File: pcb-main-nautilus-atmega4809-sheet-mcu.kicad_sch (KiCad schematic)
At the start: 20 parts, among them SW1 PTS645SH43SMTR92 LFS, U4 ATmega4809-A

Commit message: Update schematic annotations
Supports #2.
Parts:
- renumbered R13 to R12, R14 to R13, R12 to R14
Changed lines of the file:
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@@
   (symbol (lib_id "Device:R_Small") (at 66.04 113.03 180) (unit 1)
     (in_bom yes) (on_board yes) (fields_autoplaced)
-    (property "Reference" "R12" (id 0) (at 68.58 111.7599 0)
+    (property "Reference" "R14" (id 0) (at 68.58 111.7599 0)
       (effects (font (size 1.27 1.27)) (justify right))
     )
@@
   (symbol (lib_id "Device:R_Small") (at 167.64 105.41 0) (unit 1)
     (in_bom yes) (on_board yes) (fields_autoplaced)
-    (property "Reference" "R13" (id 0) (at 170.18 104.1399 0)
+    (property "Reference" "R12" (id 0) (at 170.18 104.1399 0)
       (effects (font (size 1.27 1.27)) (justify left))
     )
@@
   (symbol (lib_id "Device:R_Small") (at 182.88 105.41 0) (unit 1)
     (in_bom yes) (on_board yes) (fields_autoplaced)
-    (property "Reference" "R14" (id 0) (at 185.42 104.1399 0)
-      (effects (font (size 1.27 1.27)) (justify left))
-    )
+    (property "Reference" "R13" (id 0) (at 185.42 104.1399 0)
+      (effects (font (size 1.27 1.27)) (justify left))
+    )

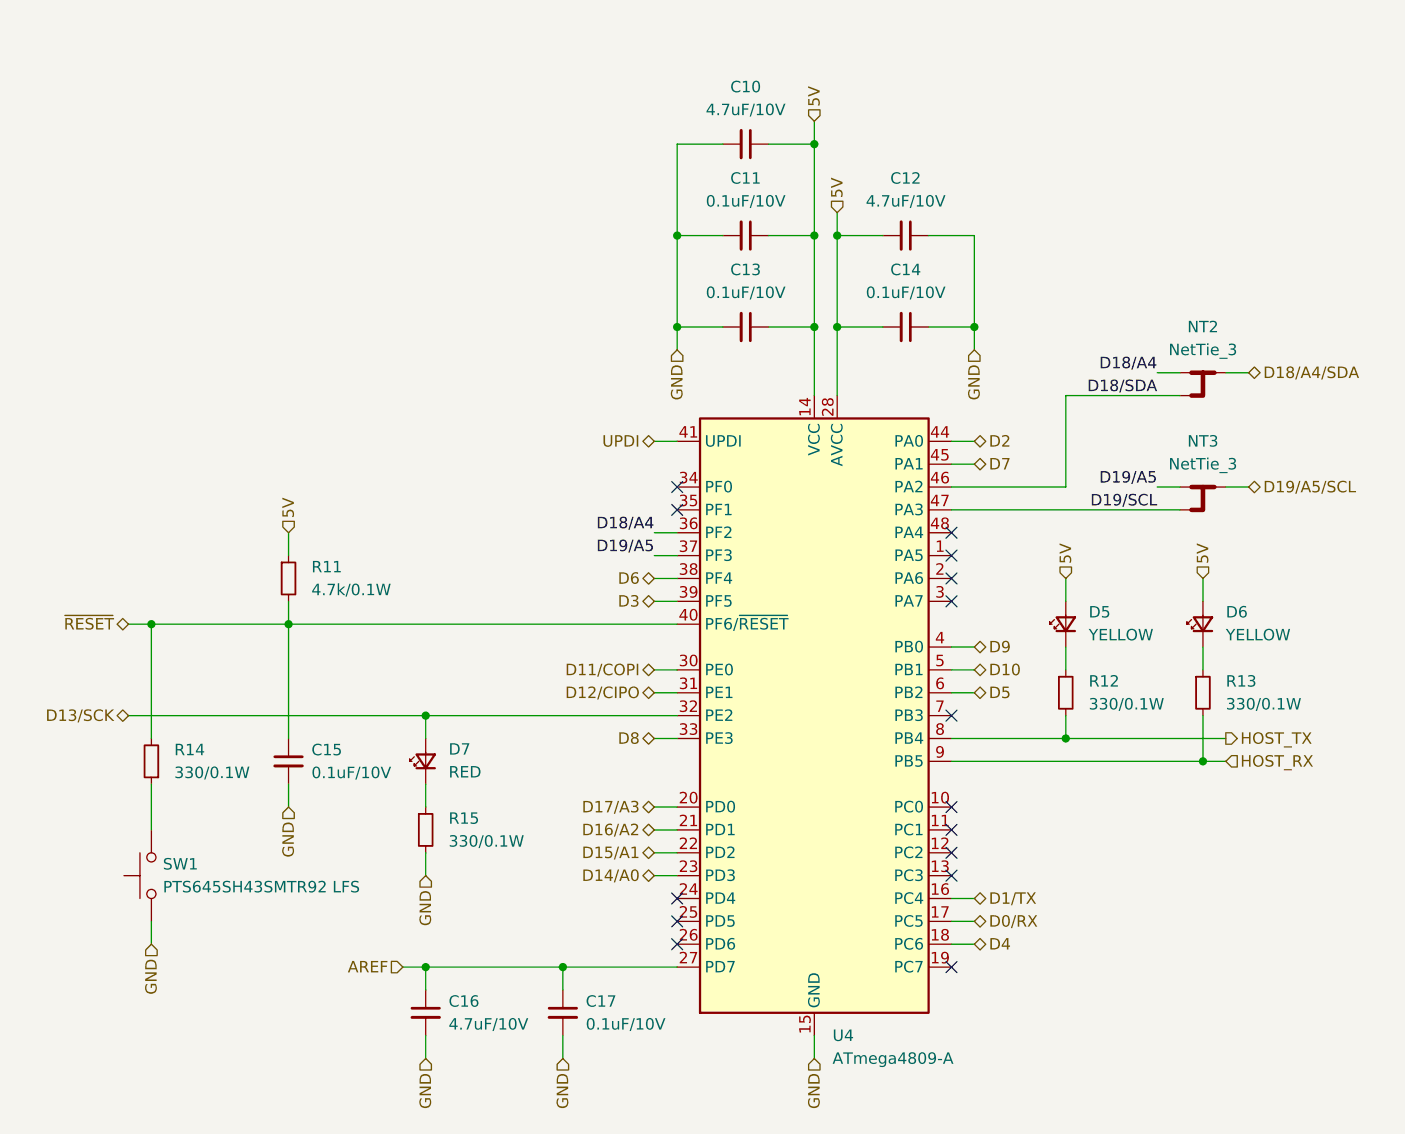
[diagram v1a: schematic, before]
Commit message: Connect root sheet
Supports #2.
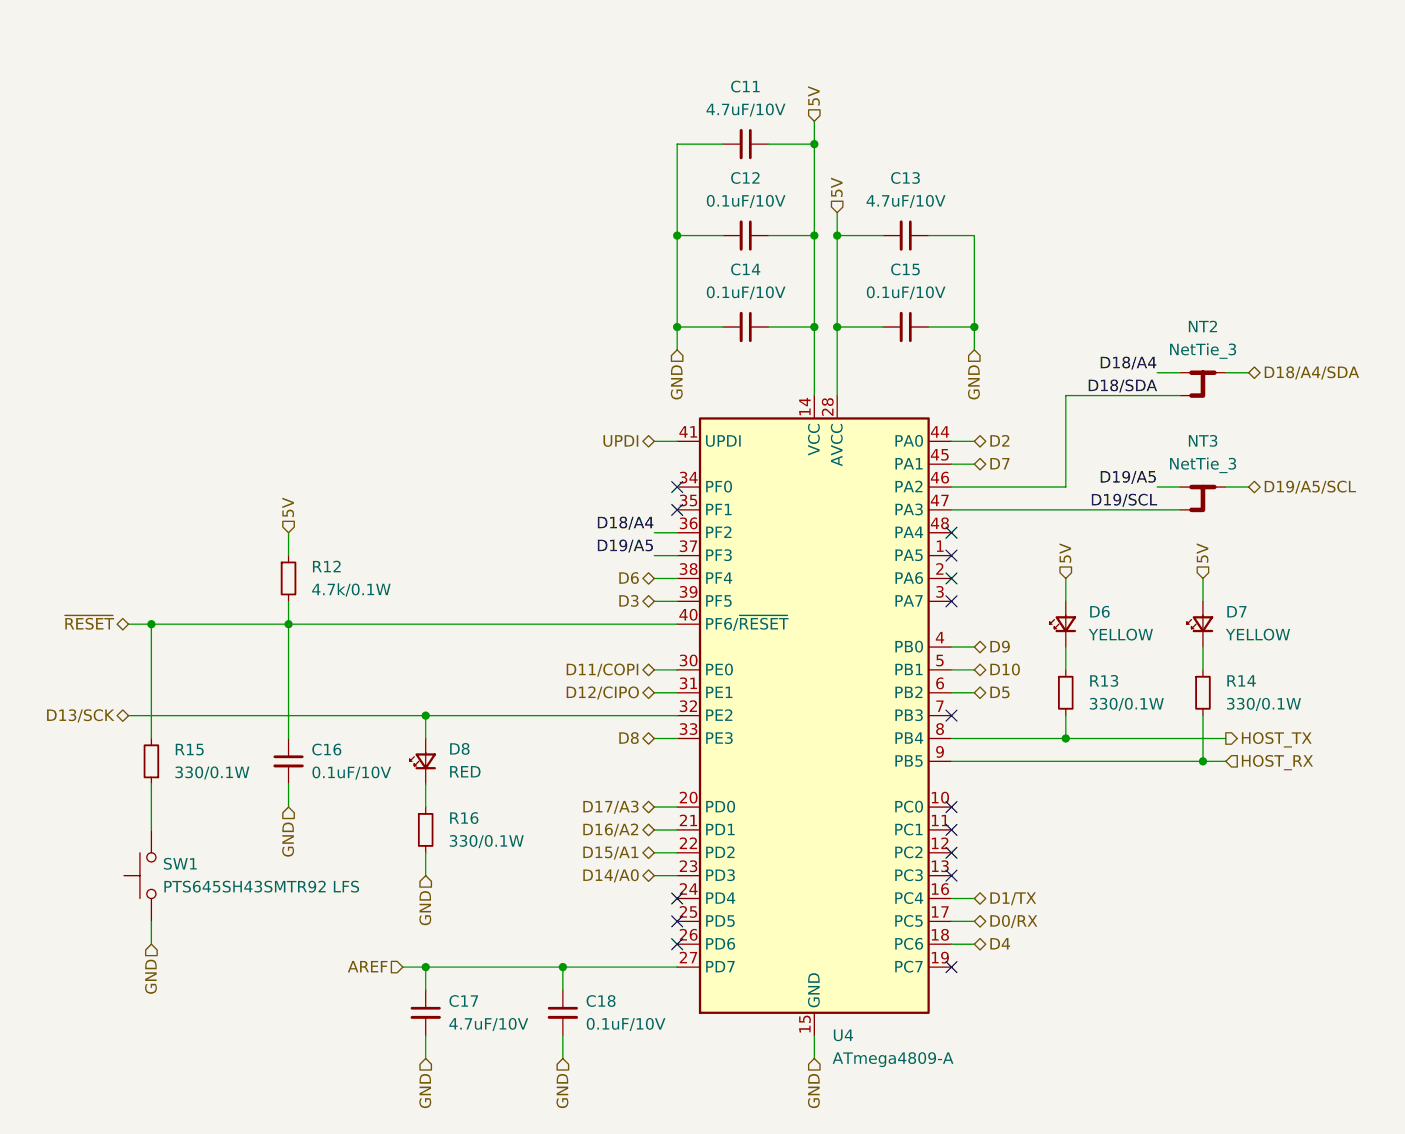
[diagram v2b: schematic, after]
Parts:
- renumbered C10 to C11, C11 to C12, C12 to C13, C13 to C14, C14 to C15, C15 to C16, C16 to C17, C17 to C18, D5 to D6, D6 to D7, D7 to D8, R11 to R12, R12 to R13, R13 to R14, R14 to R15, R15 to R16
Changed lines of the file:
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@@
   (symbol (lib_id "Device:R_Small") (at 96.52 120.65 0) (unit 1)
     (in_bom yes) (on_board yes) (fields_autoplaced)
-    (property "Reference" "R15" (id 0) (at 99.06 119.3799 0)
+    (property "Reference" "R16" (id 0) (at 99.06 119.3799 0)
       (effects (font (size 1.27 1.27)) (justify left))
     )
@@
   (symbol (lib_id "Device:C_Small") (at 111.76 140.97 0) (unit 1)
     (in_bom yes) (on_board yes) (fields_autoplaced)
-    (property "Reference" "C17" (id 0) (at 114.3 139.7062 0)
+    (property "Reference" "C18" (id 0) (at 114.3 139.7062 0)
       (effects (font (size 1.27 1.27)) (justify left))
     )
@@
   (symbol (lib_id "Device:C_Small") (at 149.86 64.77 270) (unit 1)
     (in_bom yes) (on_board yes) (fields_autoplaced)
-    (property "Reference" "C14" (id 0) (at 149.8536 58.42 90))
+    (property "Reference" "C15" (id 0) (at 149.8536 58.42 90))
     (property "Value" "0.1uF/10V" (id 1) (at 149.8536 60.96 90))
     (property "Footprint" "Capacitor_SMD:C_0603_1608Metric_Pad1.08x0.95mm_HandSolder" (id 2) (at 149.86 64.77 0)
@@
   (symbol (lib_id "Device:C_Small") (at 132.08 64.77 270) (unit 1)
     (in_bom yes) (on_board yes) (fields_autoplaced)
-    (property "Reference" "C13" (id 0) (at 132.0736 58.42 90))
+    (property "Reference" "C14" (id 0) (at 132.0736 58.42 90))
     (property "Value" "0.1uF/10V" (id 1) (at 132.0736 60.96 90))
     (property "Footprint" "Capacitor_SMD:C_0603_1608Metric_Pad1.08x0.95mm_HandSolder" (id 2) (at 132.08 64.77 0)
@@
   (symbol (lib_id "Device:R_Small") (at 66.04 113.03 180) (unit 1)
     (in_bom yes) (on_board yes) (fields_autoplaced)
-    (property "Reference" "R14" (id 0) (at 68.58 111.7599 0)
+    (property "Reference" "R15" (id 0) (at 68.58 111.7599 0)
       (effects (font (size 1.27 1.27)) (justify right))
     )
@@
   (symbol (lib_id "Device:C_Small") (at 96.52 140.97 0) (unit 1)
     (in_bom yes) (on_board yes) (fields_autoplaced)
-    (property "Reference" "C16" (id 0) (at 99.06 139.7062 0)
+    (property "Reference" "C17" (id 0) (at 99.06 139.7062 0)
       (effects (font (size 1.27 1.27)) (justify left))
     )
@@
   (symbol (lib_id "Device:C_Small") (at 81.28 113.03 0) (unit 1)
     (in_bom yes) (on_board yes) (fields_autoplaced)
-    (property "Reference" "C15" (id 0) (at 83.82 111.7662 0)
+    (property "Reference" "C16" (id 0) (at 83.82 111.7662 0)
       (effects (font (size 1.27 1.27)) (justify left))
     )
@@
   (symbol (lib_id "Device:LED_Small") (at 167.64 97.79 90) (unit 1)
     (in_bom yes) (on_board yes) (fields_autoplaced)
-    (property "Reference" "D5" (id 0) (at 170.18 96.4564 90)
+    (property "Reference" "D6" (id 0) (at 170.18 96.4564 90)
       (effects (font (size 1.27 1.27)) (justify right))
     )
@@
   (symbol (lib_id "Device:R_Small") (at 167.64 105.41 0) (unit 1)
     (in_bom yes) (on_board yes) (fields_autoplaced)
-    (property "Reference" "R12" (id 0) (at 170.18 104.1399 0)
+    (property "Reference" "R13" (id 0) (at 170.18 104.1399 0)
       (effects (font (size 1.27 1.27)) (justify left))
     )
@@
   (symbol (lib_id "Device:LED_Small") (at 96.52 113.03 90) (unit 1)
     (in_bom yes) (on_board yes) (fields_autoplaced)
-    (property "Reference" "D7" (id 0) (at 99.06 111.6964 90)
+    (property "Reference" "D8" (id 0) (at 99.06 111.6964 90)
       (effects (font (size 1.27 1.27)) (justify right))
     )
@@
   (symbol (lib_id "Device:C_Small") (at 132.08 54.61 270) (unit 1)
     (in_bom yes) (on_board yes) (fields_autoplaced)
-    (property "Reference" "C11" (id 0) (at 132.0736 48.26 90))
+    (property "Reference" "C12" (id 0) (at 132.0736 48.26 90))
     (property "Value" "0.1uF/10V" (id 1) (at 132.0736 50.8 90))
     (property "Footprint" "Capacitor_SMD:C_0603_1608Metric_Pad1.08x0.95mm_HandSolder" (id 2) (at 132.08 54.61 0)
@@
   (symbol (lib_id "Device:C_Small") (at 132.08 44.45 270) (unit 1)
     (in_bom yes) (on_board yes) (fields_autoplaced)
-    (property "Reference" "C10" (id 0) (at 132.0736 38.1 90))
+    (property "Reference" "C11" (id 0) (at 132.0736 38.1 90))
     (property "Value" "4.7uF/10V" (id 1) (at 132.0736 40.64 90))
     (property "Footprint" "Capacitor_SMD:C_0603_1608Metric_Pad1.08x0.95mm_HandSolder" (id 2) (at 132.08 44.45 0)
@@
   (symbol (lib_id "Device:R_Small") (at 182.88 105.41 0) (unit 1)
     (in_bom yes) (on_board yes) (fields_autoplaced)
-    (property "Reference" "R13" (id 0) (at 185.42 104.1399 0)
+    (property "Reference" "R14" (id 0) (at 185.42 104.1399 0)
       (effects (font (size 1.27 1.27)) (justify left))
     )
@@
   (symbol (lib_id "Device:LED_Small") (at 182.88 97.79 90) (unit 1)
     (in_bom yes) (on_board yes) (fields_autoplaced)
-    (property "Reference" "D6" (id 0) (at 185.42 96.4564 90)
+    (property "Reference" "D7" (id 0) (at 185.42 96.4564 90)
       (effects (font (size 1.27 1.27)) (justify right))
     )
@@
   (symbol (lib_id "Device:C_Small") (at 149.86 54.61 270) (unit 1)
     (in_bom yes) (on_board yes) (fields_autoplaced)
-    (property "Reference" "C12" (id 0) (at 149.8536 48.26 90))
+    (property "Reference" "C13" (id 0) (at 149.8536 48.26 90))
     (property "Value" "4.7uF/10V" (id 1) (at 149.8536 50.8 90))
     (property "Footprint" "Capacitor_SMD:C_0603_1608Metric_Pad1.08x0.95mm_HandSolder" (id 2) (at 149.86 54.61 0)
@@
   (symbol (lib_id "Device:R_Small") (at 81.28 92.71 0) (unit 1)
     (in_bom yes) (on_board yes) (fields_autoplaced)
-    (property "Reference" "R11" (id 0) (at 83.82 91.4399 0)
-      (effects (font (size 1.27 1.27)) (justify left))
-    )
+    (property "Reference" "R12" (id 0) (at 83.82 91.4399 0)
+      (effects (font (size 1.27 1.27)) (justify left))
+    )

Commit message: Nest level shifter sheets under UPDI programmer and bridge sheet
Supports #2.
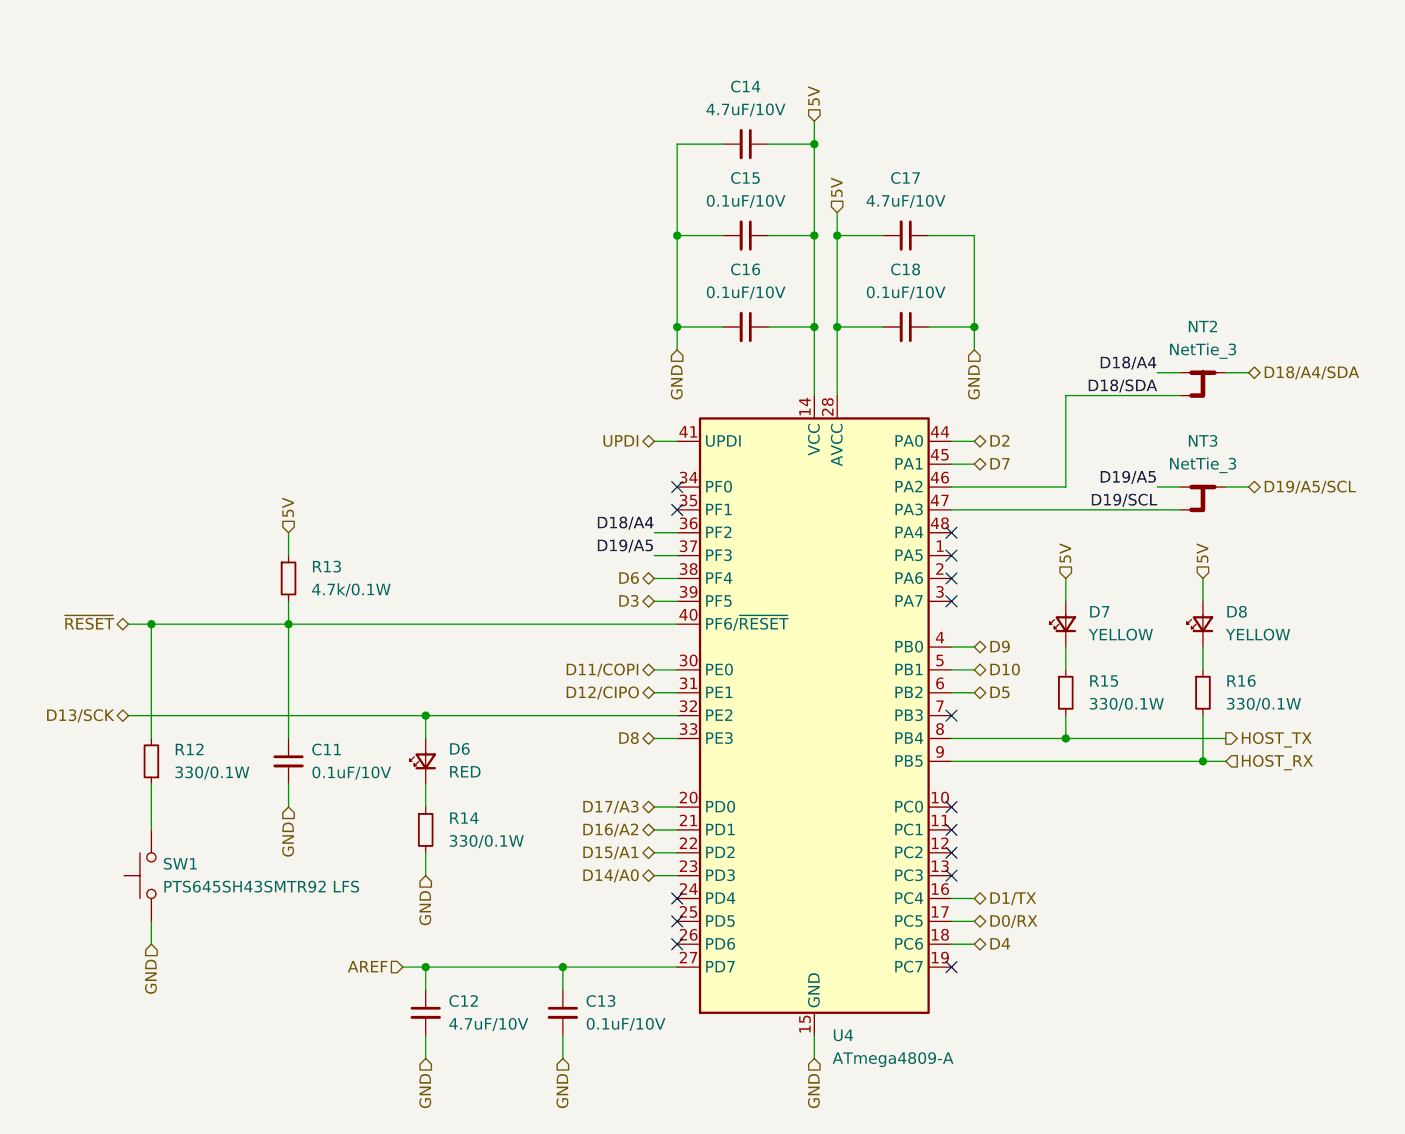
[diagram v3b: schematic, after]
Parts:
- renumbered C16 to C11, C17 to C12, C18 to C13, C11 to C14, C12 to C15, C14 to C16, C13 to C17, C15 to C18, D8 to D6, D6 to D7, D7 to D8, R15 to R12, R12 to R13, R16 to R14, R13 to R15, R14 to R16
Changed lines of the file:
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@@
   (symbol (lib_id "Device:R_Small") (at 96.52 120.65 0) (unit 1)
     (in_bom yes) (on_board yes) (fields_autoplaced)
-    (property "Reference" "R16" (id 0) (at 99.06 119.3799 0)
+    (property "Reference" "R14" (id 0) (at 99.06 119.3799 0)
       (effects (font (size 1.27 1.27)) (justify left))
     )
@@
   (symbol (lib_id "Device:C_Small") (at 111.76 140.97 0) (unit 1)
     (in_bom yes) (on_board yes) (fields_autoplaced)
-    (property "Reference" "C18" (id 0) (at 114.3 139.7062 0)
+    (property "Reference" "C13" (id 0) (at 114.3 139.7062 0)
       (effects (font (size 1.27 1.27)) (justify left))
     )
@@
   (symbol (lib_id "Device:C_Small") (at 149.86 64.77 270) (unit 1)
     (in_bom yes) (on_board yes) (fields_autoplaced)
-    (property "Reference" "C15" (id 0) (at 149.8536 58.42 90))
+    (property "Reference" "C18" (id 0) (at 149.8536 58.42 90))
     (property "Value" "0.1uF/10V" (id 1) (at 149.8536 60.96 90))
     (property "Footprint" "Capacitor_SMD:C_0603_1608Metric_Pad1.08x0.95mm_HandSolder" (id 2) (at 149.86 64.77 0)
@@
   (symbol (lib_id "Device:C_Small") (at 132.08 64.77 270) (unit 1)
     (in_bom yes) (on_board yes) (fields_autoplaced)
-    (property "Reference" "C14" (id 0) (at 132.0736 58.42 90))
+    (property "Reference" "C16" (id 0) (at 132.0736 58.42 90))
     (property "Value" "0.1uF/10V" (id 1) (at 132.0736 60.96 90))
     (property "Footprint" "Capacitor_SMD:C_0603_1608Metric_Pad1.08x0.95mm_HandSolder" (id 2) (at 132.08 64.77 0)
@@
   (symbol (lib_id "Device:R_Small") (at 66.04 113.03 180) (unit 1)
     (in_bom yes) (on_board yes) (fields_autoplaced)
-    (property "Reference" "R15" (id 0) (at 68.58 111.7599 0)
+    (property "Reference" "R12" (id 0) (at 68.58 111.7599 0)
       (effects (font (size 1.27 1.27)) (justify right))
     )
@@
   (symbol (lib_id "Device:C_Small") (at 96.52 140.97 0) (unit 1)
     (in_bom yes) (on_board yes) (fields_autoplaced)
-    (property "Reference" "C17" (id 0) (at 99.06 139.7062 0)
+    (property "Reference" "C12" (id 0) (at 99.06 139.7062 0)
       (effects (font (size 1.27 1.27)) (justify left))
     )
@@
   (symbol (lib_id "Device:C_Small") (at 81.28 113.03 0) (unit 1)
     (in_bom yes) (on_board yes) (fields_autoplaced)
-    (property "Reference" "C16" (id 0) (at 83.82 111.7662 0)
+    (property "Reference" "C11" (id 0) (at 83.82 111.7662 0)
       (effects (font (size 1.27 1.27)) (justify left))
     )
@@
   (symbol (lib_id "Device:LED_Small") (at 167.64 97.79 90) (unit 1)
     (in_bom yes) (on_board yes) (fields_autoplaced)
-    (property "Reference" "D6" (id 0) (at 170.18 96.4564 90)
+    (property "Reference" "D7" (id 0) (at 170.18 96.4564 90)
       (effects (font (size 1.27 1.27)) (justify right))
     )
@@
   (symbol (lib_id "Device:R_Small") (at 167.64 105.41 0) (unit 1)
     (in_bom yes) (on_board yes) (fields_autoplaced)
-    (property "Reference" "R13" (id 0) (at 170.18 104.1399 0)
+    (property "Reference" "R15" (id 0) (at 170.18 104.1399 0)
       (effects (font (size 1.27 1.27)) (justify left))
     )
@@
   (symbol (lib_id "Device:LED_Small") (at 96.52 113.03 90) (unit 1)
     (in_bom yes) (on_board yes) (fields_autoplaced)
-    (property "Reference" "D8" (id 0) (at 99.06 111.6964 90)
+    (property "Reference" "D6" (id 0) (at 99.06 111.6964 90)
       (effects (font (size 1.27 1.27)) (justify right))
     )
@@
   (symbol (lib_id "Device:C_Small") (at 132.08 54.61 270) (unit 1)
     (in_bom yes) (on_board yes) (fields_autoplaced)
-    (property "Reference" "C12" (id 0) (at 132.0736 48.26 90))
+    (property "Reference" "C15" (id 0) (at 132.0736 48.26 90))
     (property "Value" "0.1uF/10V" (id 1) (at 132.0736 50.8 90))
     (property "Footprint" "Capacitor_SMD:C_0603_1608Metric_Pad1.08x0.95mm_HandSolder" (id 2) (at 132.08 54.61 0)
@@
   (symbol (lib_id "Device:C_Small") (at 132.08 44.45 270) (unit 1)
     (in_bom yes) (on_board yes) (fields_autoplaced)
-    (property "Reference" "C11" (id 0) (at 132.0736 38.1 90))
+    (property "Reference" "C14" (id 0) (at 132.0736 38.1 90))
     (property "Value" "4.7uF/10V" (id 1) (at 132.0736 40.64 90))
     (property "Footprint" "Capacitor_SMD:C_0603_1608Metric_Pad1.08x0.95mm_HandSolder" (id 2) (at 132.08 44.45 0)
@@
   (symbol (lib_id "Device:R_Small") (at 182.88 105.41 0) (unit 1)
     (in_bom yes) (on_board yes) (fields_autoplaced)
-    (property "Reference" "R14" (id 0) (at 185.42 104.1399 0)
+    (property "Reference" "R16" (id 0) (at 185.42 104.1399 0)
       (effects (font (size 1.27 1.27)) (justify left))
     )
@@
   (symbol (lib_id "Device:LED_Small") (at 182.88 97.79 90) (unit 1)
     (in_bom yes) (on_board yes) (fields_autoplaced)
-    (property "Reference" "D7" (id 0) (at 185.42 96.4564 90)
+    (property "Reference" "D8" (id 0) (at 185.42 96.4564 90)
       (effects (font (size 1.27 1.27)) (justify right))
     )
@@
   (symbol (lib_id "Device:C_Small") (at 149.86 54.61 270) (unit 1)
     (in_bom yes) (on_board yes) (fields_autoplaced)
-    (property "Reference" "C13" (id 0) (at 149.8536 48.26 90))
+    (property "Reference" "C17" (id 0) (at 149.8536 48.26 90))
     (property "Value" "4.7uF/10V" (id 1) (at 149.8536 50.8 90))
     (property "Footprint" "Capacitor_SMD:C_0603_1608Metric_Pad1.08x0.95mm_HandSolder" (id 2) (at 149.86 54.61 0)
@@
   (symbol (lib_id "Device:R_Small") (at 81.28 92.71 0) (unit 1)
     (in_bom yes) (on_board yes) (fields_autoplaced)
-    (property "Reference" "R12" (id 0) (at 83.82 91.4399 0)
-      (effects (font (size 1.27 1.27)) (justify left))
-    )
+    (property "Reference" "R13" (id 0) (at 83.82 91.4399 0)
+      (effects (font (size 1.27 1.27)) (justify left))
+    )
